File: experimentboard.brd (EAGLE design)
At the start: 110.5 x 100 mm, 172 parts, among them IC1 TL072P, IC2 LM317, IC3 LM337, IC4 TL072P, IC5 TL072P, IC6 TL072P, P1 PLR135/T9, P9 P9, U1 PCM1690, U2 DIR9001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

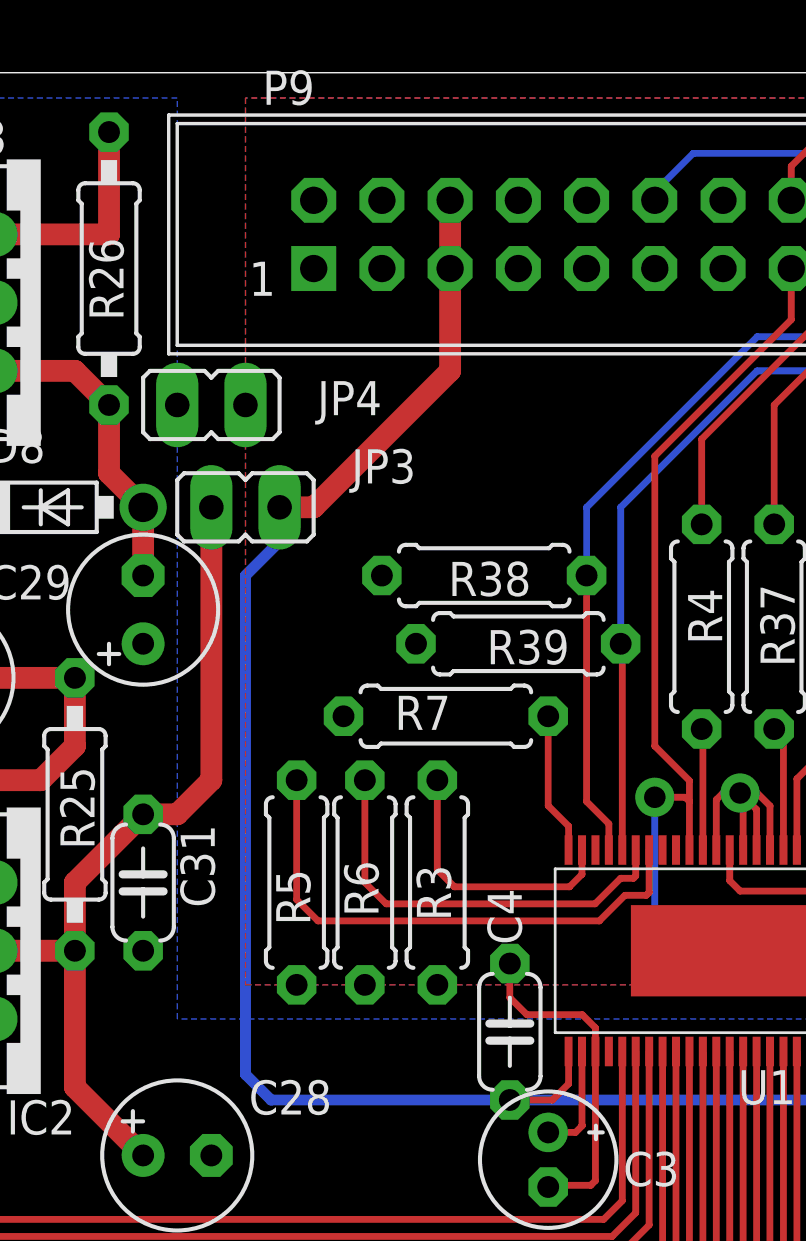
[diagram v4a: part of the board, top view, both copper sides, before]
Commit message: Fixed bug in joining VCC and V+
I now use a 0 Ohm resistor to join VCC and V+. The jumper is also fixed,
because I had erroneously tied the PCM1690 VCC to VDD_5V on the beagle
bone, which means the beagle bone's adapter would have powered the
PCM1690.
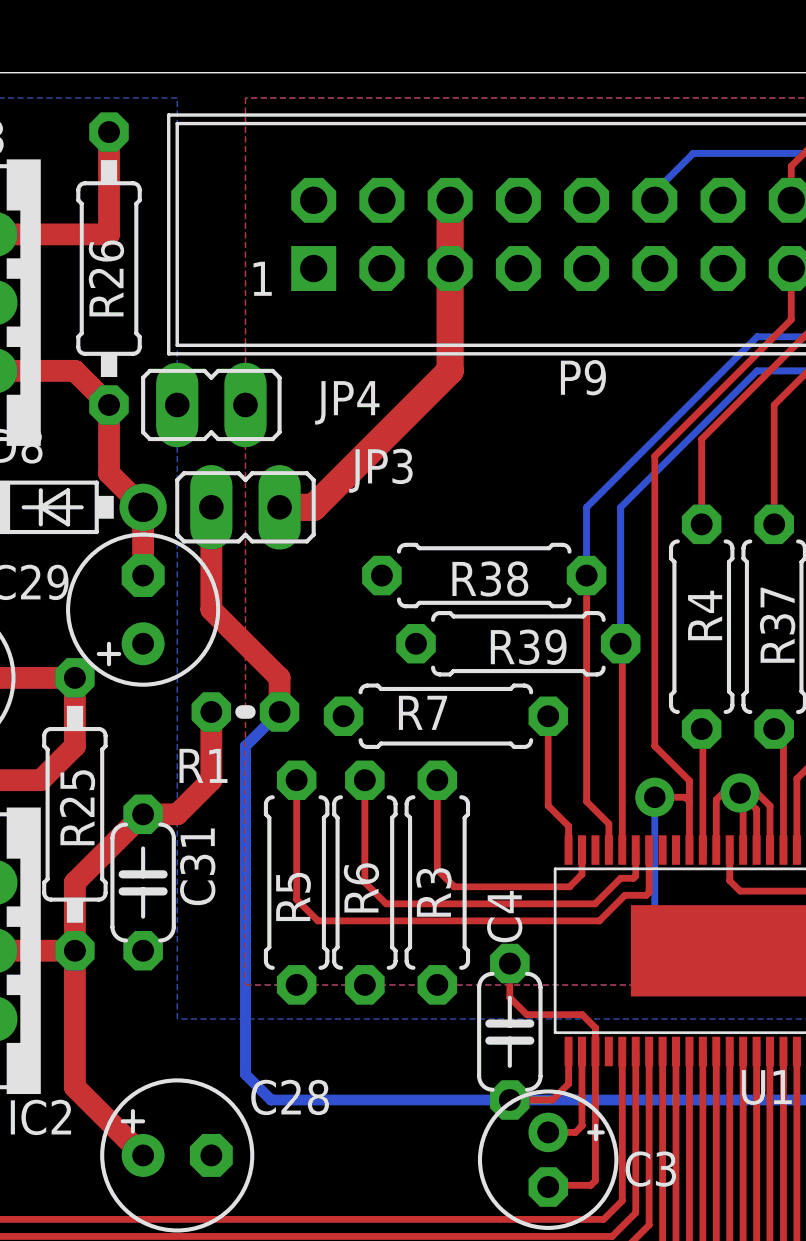
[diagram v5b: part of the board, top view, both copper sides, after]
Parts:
- added R1: 0, rcl:0204V
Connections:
- new net VDD_5V: JP3.1, P9.5, P9.6
- net V+: now also R1.1; no longer JP3.2
- net VCC: now also JP3.2, R1.2; no longer JP3.1, P9.5, P9.6
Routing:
- net VDD_5V: track 0.00 -> 14.8 mm
- net VCC: track 74.1 -> 60.4 mm
- net V+: track 203.1 -> 195.5 mm
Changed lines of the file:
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@@
 <attribute name="VALUE" x="52.15255" y="67.564" size="1.27" layer="27" ratio="10" rot="R90"/>
 </element>
-<element name="P9" library="0000halfgaar" package="HEADERS23-2" value="P9" x="52.07" y="93.98"/>
+<element name="P9" library="0000halfgaar" package="HEADERS23-2" value="P9" x="52.07" y="93.98" smashed="yes">
+<attribute name="NAME" x="56.03875" y="88.011" size="1.27" layer="25" ratio="10"/>
+<attribute name="VALUE" x="89.535" y="87.884" size="1.27" layer="27" ratio="10"/>
+</element>
 <element name="R35" library="rcl" package="0207/7" value="22" x="69.5325" y="79.375" smashed="yes" rot="R270">
 <attribute name="NAME" x="69.18325" y="81.28" size="1.27" layer="25" ratio="10" rot="R270"/>
@@
 <attribute name="NAME" x="49.53" y="88.519" size="1.27" layer="25" ratio="10" rot="R180"/>
 <attribute name="VALUE" x="45.72" y="90.551" size="1.27" layer="27" ratio="10" rot="R180"/>
+</element>
+<element name="R1" library="rcl" package="0204V" value="0" x="44.45" y="76.2" smashed="yes">
+<attribute name="NAME" x="41.84015" y="73.5584" size="1.27" layer="25" ratio="10"/>
+<attribute name="VALUE" x="42.3164" y="73.8886" size="1.27" layer="27" ratio="10"/>
 </element>
 </elements>
@@
 <contactref element="U1" pad="47"/>
 <contactref element="U1" pad="25"/>
-<contactref element="P9" pad="6"/>
-<contactref element="P9" pad="5"/>
-<contactref element="JP3" pad="1"/>
-<wire x1="45.72" y1="83.82" x2="45.72" y2="82.55" width="0.4064" layer="16"/>
-<wire x1="45.72" y1="82.55" x2="44.45" y2="81.28" width="0.4064" layer="16"/>
-<wire x1="44.45" y1="81.28" x2="44.45" y2="62.70625" width="0.4064" layer="16"/>
+<wire x1="44.45" y1="74.93" x2="44.45" y2="62.70625" width="0.4064" layer="16"/>
 <wire x1="44.45" y1="62.70625" x2="45.4025" y2="61.75375" width="0.4064" layer="16"/>
 <wire x1="45.4025" y1="61.75375" x2="54.2925" y2="61.75375" width="0.4064" layer="16"/>
@@
 <wire x1="56.48" y1="62.35375" x2="55.88" y2="61.75375" width="0.254" layer="1"/>
 <wire x1="55.88" y1="61.75375" x2="54.2925" y2="61.75375" width="0.254" layer="1"/>
-<wire x1="52.07" y1="92.71" x2="52.07" y2="95.25" width="0.8128" layer="1"/>
-<wire x1="45.72" y1="83.82" x2="46.99" y2="83.82" width="0.8128" layer="1"/>
-<wire x1="46.99" y1="83.82" x2="52.07" y2="88.9" width="0.8128" layer="1"/>
-<wire x1="52.07" y1="88.9" x2="52.07" y2="92.71" width="0.8128" layer="1"/>
 <wire x1="69.85" y1="61.75375" x2="70.32625" y2="62.23" width="0.4064" layer="16"/>
 <wire x1="70.32625" y1="62.23" x2="70.32625" y2="63.65875" width="0.4064" layer="16"/>
+<contactref element="JP3" pad="2"/>
+<contactref element="R1" pad="2"/>
+<wire x1="44.45" y1="74.93" x2="45.72" y2="76.2" width="0.4064" layer="16"/>
+<wire x1="45.72" y1="76.2" x2="45.72" y2="77.47" width="0.8128" layer="1"/>
+<wire x1="45.72" y1="77.47" x2="43.18" y2="80.01" width="0.8128" layer="1"/>
+<wire x1="43.18" y1="80.01" x2="43.18" y2="83.82" width="0.8128" layer="1"/>
 </signal>
 <signal name="3V3">
@@
 <wire x1="54.61" y1="10.795" x2="54.61" y2="9.8425" width="0.6096" layer="16"/>
 <wire x1="80.01" y1="10.795" x2="80.01" y2="9.8425" width="0.6096" layer="16"/>
-<contactref element="JP3" pad="2"/>
 <wire x1="40.64" y1="72.39" x2="41.91" y2="72.39" width="0.8128" layer="1"/>
 <wire x1="41.91" y1="72.39" x2="43.18" y2="73.66" width="0.8128" layer="1"/>
-<wire x1="43.18" y1="73.66" x2="43.18" y2="83.82" width="0.8128" layer="1"/>
 <wire x1="26.67" y1="60.96" x2="26.67" y2="57.15" width="0.6096" layer="16"/>
 <wire x1="26.67" y1="57.15" x2="25.4" y2="55.88" width="0.6096" layer="16"/>
 <wire x1="25.4" y1="55.88" x2="15.24" y2="55.88" width="0.6096" layer="16"/>
 <wire x1="15.24" y1="55.88" x2="13.97" y2="54.61" width="0.6096" layer="16"/>
+<contactref element="R1" pad="1"/>
+<wire x1="43.18" y1="73.66" x2="43.18" y2="76.2" width="0.8128" layer="1"/>
 </signal>
 <signal name="N$39">
@@
 <wire x1="95.9485" y1="72.644" x2="96.2025" y2="72.39" width="1.016" layer="1"/>
 </signal>
+<signal name="VDD_5V">
+<contactref element="P9" pad="6"/>
+<contactref element="P9" pad="5"/>
+<contactref element="JP3" pad="1"/>
+<wire x1="52.07" y1="95.25" x2="52.07" y2="92.71" width="1.016" layer="1"/>
+<wire x1="52.07" y1="92.71" x2="52.07" y2="88.9" width="1.016" layer="1"/>
+<wire x1="52.07" y1="88.9" x2="46.99" y2="83.82" width="1.016" layer="1"/>
+<wire x1="46.99" y1="83.82" x2="45.72" y2="83.82" width="1.016" layer="1"/>
+</signal>
 </signals>

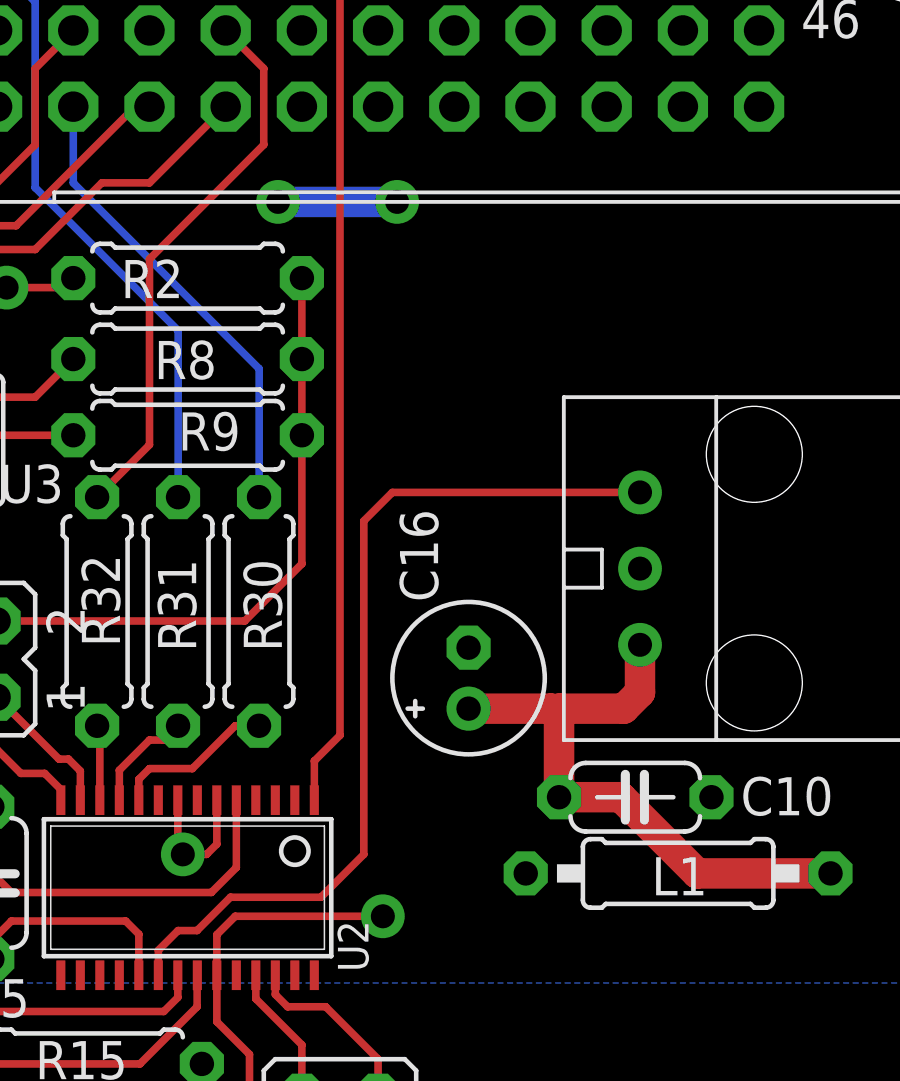
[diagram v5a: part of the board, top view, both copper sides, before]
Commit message: Removed unnecessary vias
By moving a bit of wire, the VDD plane is now more continuous.
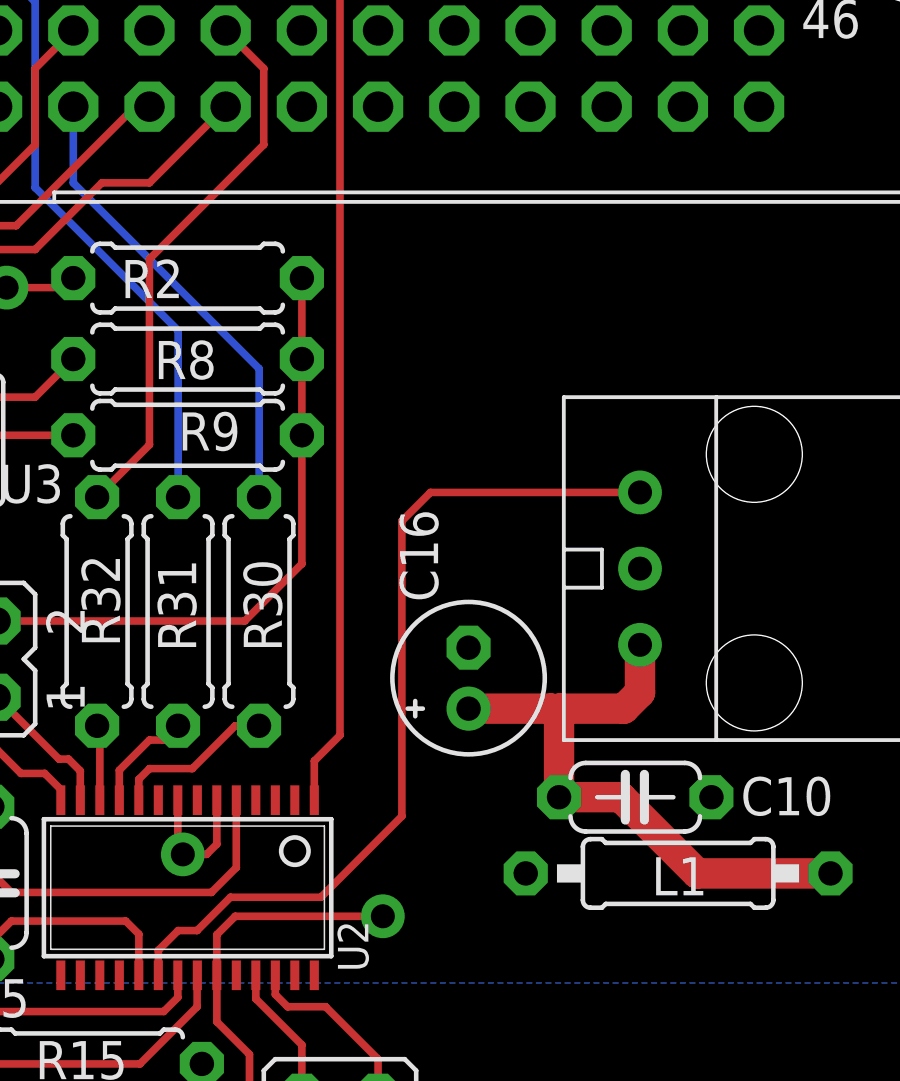
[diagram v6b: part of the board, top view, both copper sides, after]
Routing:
- net VDD: track 75.5 -> 71.5 mm, vias 2 -> 0
- net N$20: track 29.7 -> 29.0 mm
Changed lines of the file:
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@@
 <wire x1="77.31125" y1="67.15125" x2="77.31125" y2="68.58" width="0.254" layer="1"/>
 <wire x1="77.31125" y1="68.58" x2="76.914375" y2="68.976875" width="0.254" layer="1"/>
-<via x="86.83625" y="89.535" extent="1-16" drill="0.8" shape="octagon"/>
-<via x="90.805" y="89.535" extent="1-16" drill="0.8" shape="octagon"/>
-<wire x1="86.83625" y1="89.535" x2="90.805" y2="89.535" width="1.016" layer="16"/>
 <contactref element="U2" pad="24"/>
 </signal>
@@
 <contactref element="U2" pad="20"/>
 <contactref element="P1" pad="1"/>
-<wire x1="88.265" y1="66.3575" x2="89.69375" y2="67.78625" width="0.254" layer="1"/>
-<wire x1="98.90125" y1="79.85125" x2="90.64625" y2="79.85125" width="0.254" layer="1"/>
-<wire x1="89.69375" y1="78.89875" x2="89.69375" y2="67.78625" width="0.254" layer="1"/>
+<wire x1="88.265" y1="66.3575" x2="90.96375" y2="69.05625" width="0.254" layer="1"/>
+<wire x1="98.90125" y1="79.85125" x2="91.91625" y2="79.85125" width="0.254" layer="1"/>
+<wire x1="90.96375" y1="78.89875" x2="90.96375" y2="69.05625" width="0.254" layer="1"/>
 <wire x1="82.845" y1="63.7572" x2="82.845" y2="64.58875" width="0.254" layer="1"/>
 <wire x1="85.24875" y1="66.3575" x2="88.265" y2="66.3575" width="0.254" layer="1"/>
-<wire x1="90.64625" y1="79.85125" x2="89.69375" y2="78.89875" width="0.254" layer="1"/>
+<wire x1="91.91625" y1="79.85125" x2="90.96375" y2="78.89875" width="0.254" layer="1"/>
 <wire x1="85.24875" y1="66.3575" x2="84.1375" y2="65.24625" width="0.254" layer="1"/>
 <wire x1="84.1375" y1="65.24625" x2="83.5025" y2="65.24625" width="0.254" layer="1"/>

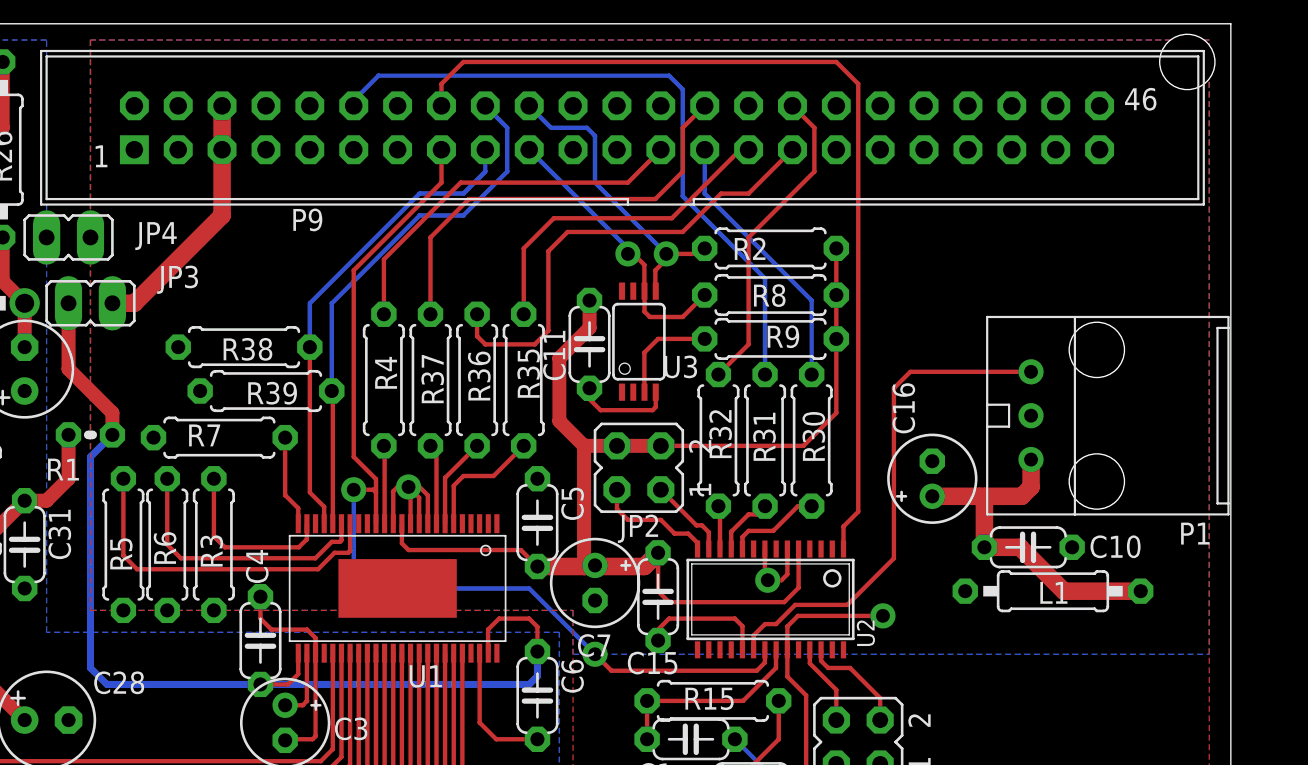
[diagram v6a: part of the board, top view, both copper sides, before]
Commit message: Added two status LEDs
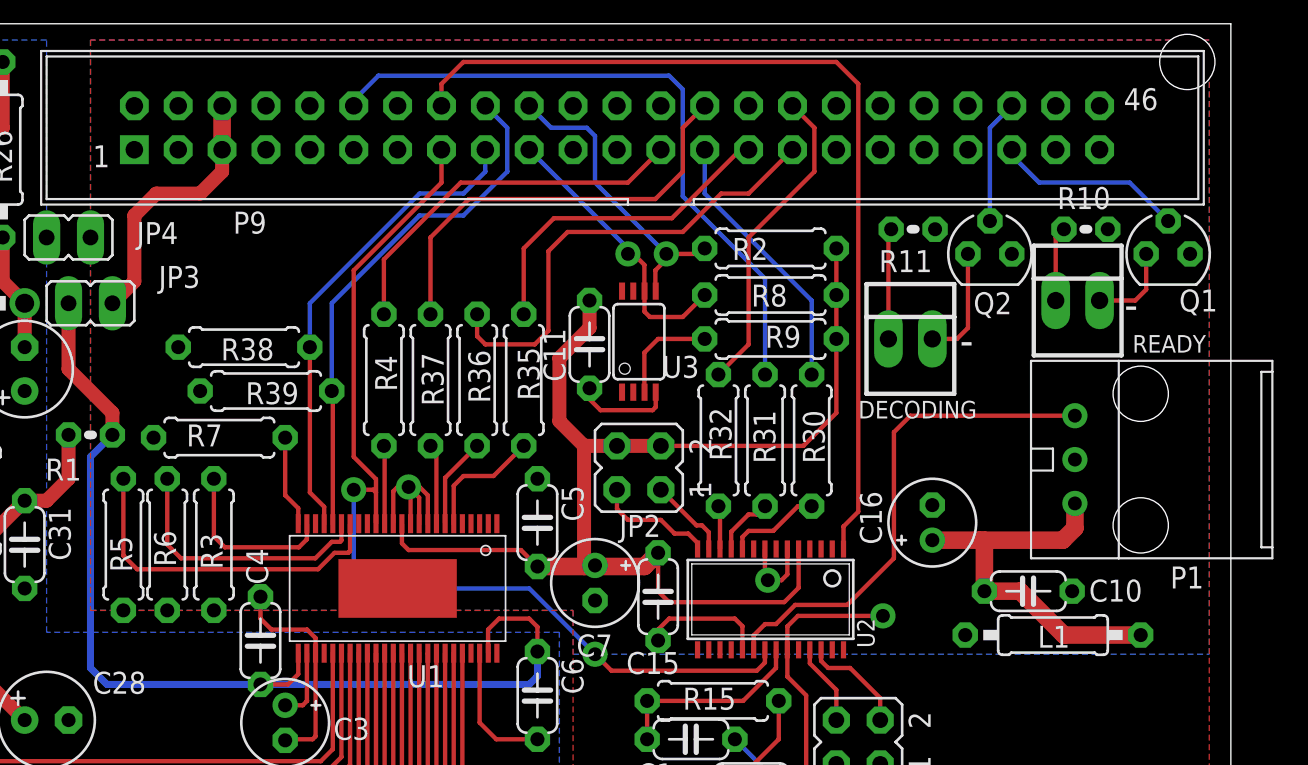
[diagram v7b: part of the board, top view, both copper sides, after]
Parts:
- added DECODING, READY: 22-23-2021, con-molex:22-23-2021
- added Q1, Q2: BS170, transistor-small-signal:SOT54E
- added R10, R11: 68, rcl:0204V
- moved P1 3.59 mm to (112.9, 69.1)
- moved L1 2.54 mm to (100.2, 64.6)
- moved C10 2.54 mm to (98.7, 67.2)
- moved C16 2.54 mm to (93.2, 71.1)
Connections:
- new net N$28: R10.1, READY.1
- new net N$4: Q1.D, READY.2
- new net N$91: DECODING.2, Q2.D
- new net N$92: DECODING.1, R11.1
- new net N$93: P9.41, Q1.G
- new net N$94: P9.42, Q2.G
- net DGND: now also Q1.S, Q2.S
- net VDD: now also R10.2, R11.2
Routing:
- net N$93: track 0.00 -> 10.9 mm
- net N$94: track 0.00 -> 7.19 mm
- net N$91: track 0.00 -> 6.61 mm
- net N$92: track 0.00 -> 6.42 mm
- net N$4: track 0.00 -> 5.03 mm
- net N$28: track 0.00 -> 4.32 mm
- net N$12: track 20.7 -> 23.1 mm
- net VDD_5V: track 14.8 -> 15.5 mm
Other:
- board text added: "-"
